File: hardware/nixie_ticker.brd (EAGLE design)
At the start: 124.1 x 49.5 mm, 12 parts

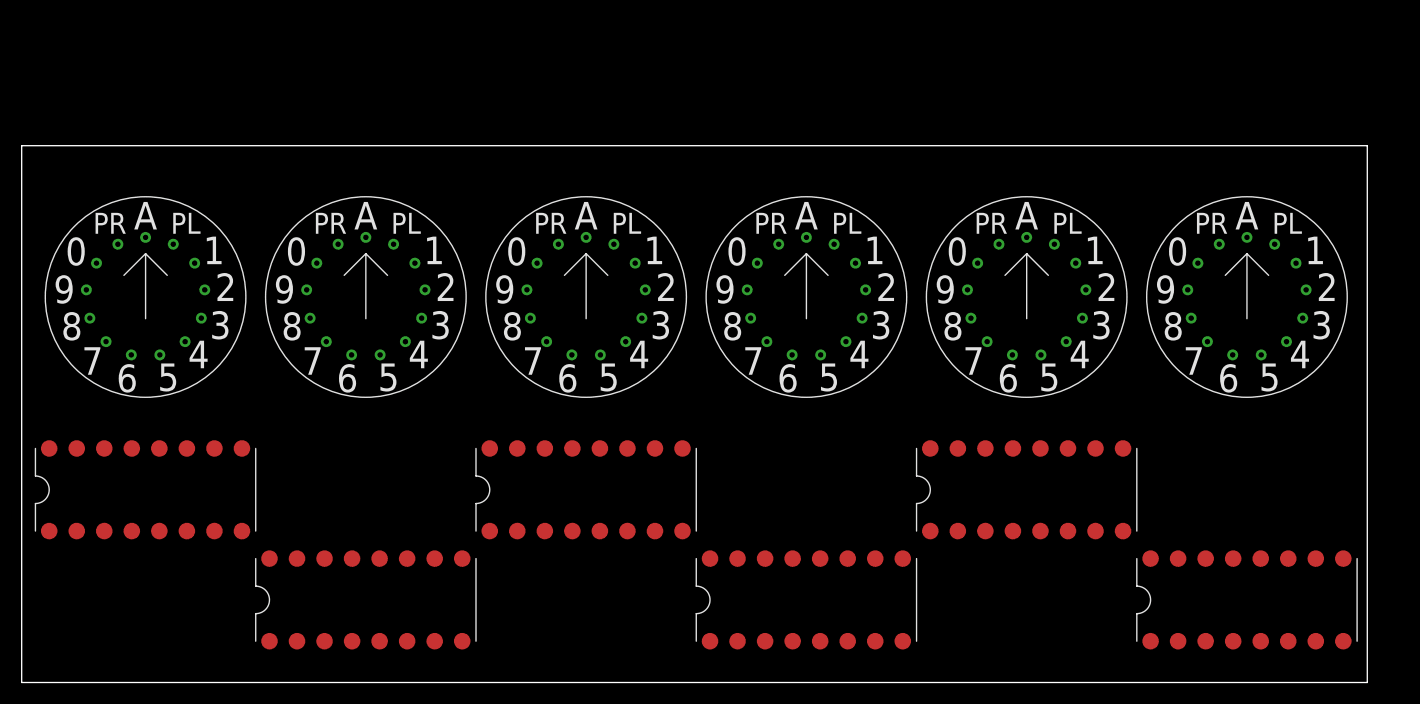
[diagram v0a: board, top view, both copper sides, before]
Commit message: Initial routing for first nixie
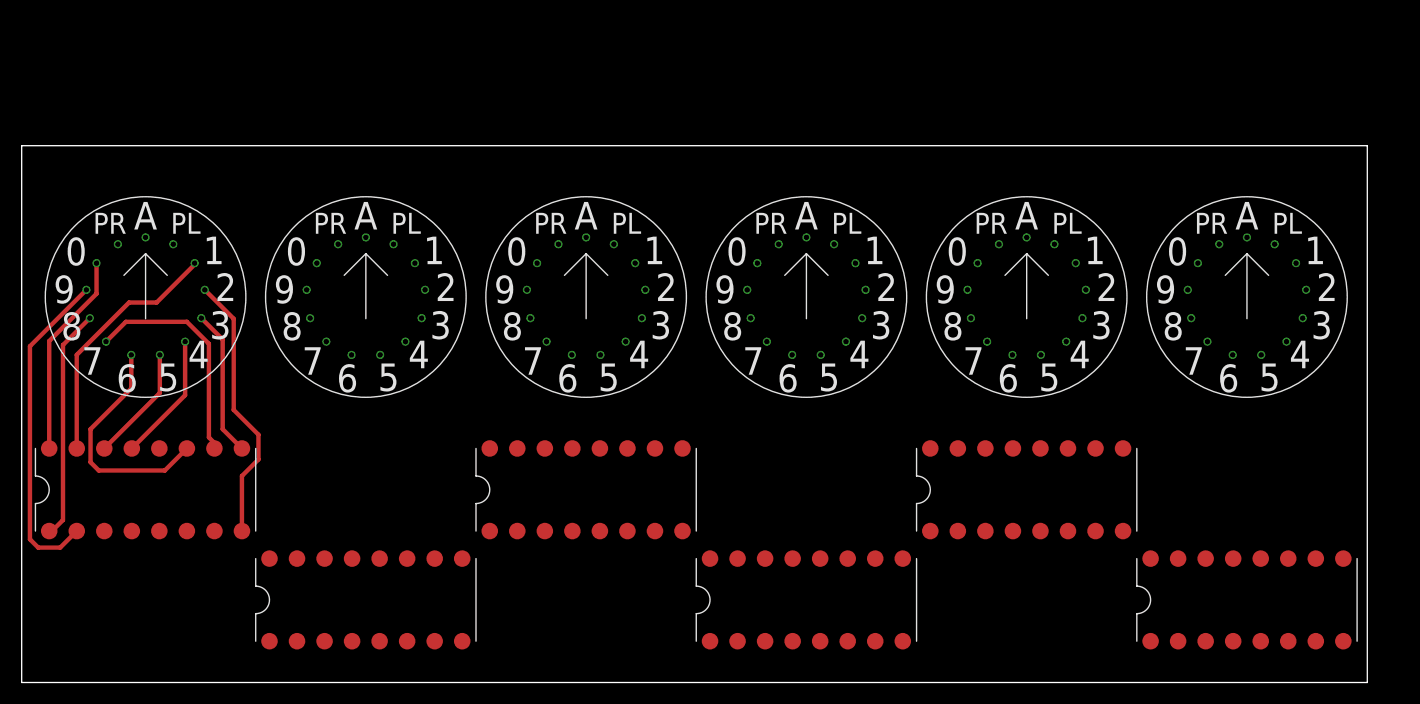
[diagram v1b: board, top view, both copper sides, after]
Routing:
- net N$10: track 0.00 -> 30.4 mm
- net N$3: track 0.00 -> 24.9 mm
- net N$2: track 0.00 -> 23.1 mm
- net N$7: track 0.00 -> 21.5 mm
- net N$9: track 0.00 -> 21.3 mm
- net N$8: track 0.00 -> 21.0 mm
- net N$1: track 0.00 -> 18.9 mm
- net N$4: track 0.00 -> 13.6 mm
- net N$5: track 0.00 -> 11.9 mm
- net N$6: track 0.00 -> 10.8 mm

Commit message: Wiring all nixie tubes using design blocks
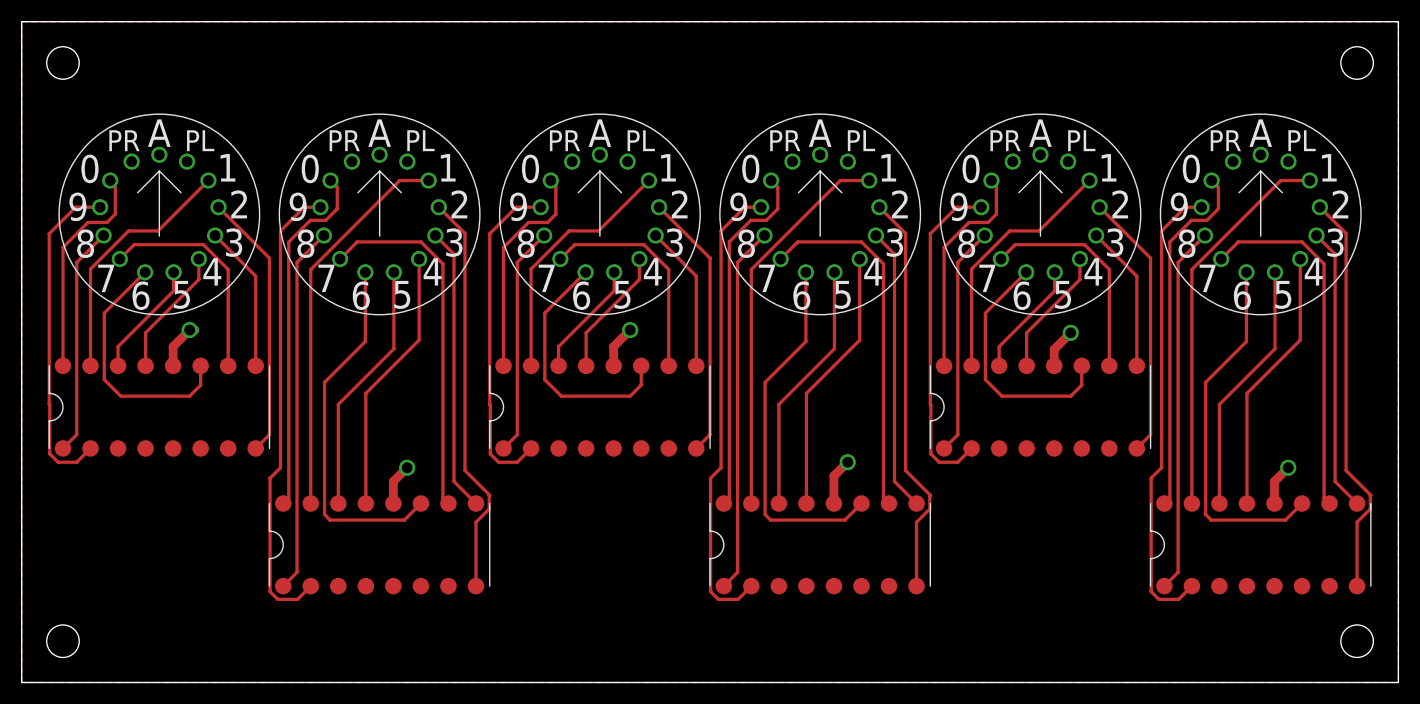
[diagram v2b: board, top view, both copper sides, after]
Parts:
- removed U$10, U$9: K155ID1, nixie_ticker:DIP-16_SMD
- removed U$3, U$4: IN14, nixie_ticker:IN14
- added U$15, U$19: IN14, nixie_ticker:IN14
- added U$16, U$20: K155ID1, nixie_ticker:DIP-16_SMD
- U$11: value K155ID1 -> IN14; device nixie_ticker:DIP-16_SMD -> nixie_ticker:IN14
- U$6: value IN14 -> K155ID1; device nixie_ticker:IN14 -> nixie_ticker:DIP-16_SMD
- moved U$6 60.5 mm to (53.3, 25.4), turned to 90 degrees
- moved U$5 40.1 mm to (53.3, 43.2)
- moved U$12 39.7 mm to (73.7, 12.7)
- moved U$11 31.8 mm to (73.7, 43.2), turned to 0 degrees
- moved U$2 7.73 mm to (33.0, 43.2)
- moved U$1 7.73 mm to (12.7, 43.2)
- moved U$7 7.73 mm to (12.7, 25.4)
- moved U$8 5.24 mm to (33.0, 12.7)
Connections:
- removed net N$21: U$3.P$12, U$9.P$16
- removed net N$22: U$3.P$3, U$9.P$15
- removed net N$23: U$3.P$4, U$9.P$8
- removed net N$24: U$3.P$5, U$9.P$9
- removed net N$25: U$3.P$6, U$9.P$13
- removed net N$26: U$3.P$7, U$9.P$14
- removed net N$27: U$3.P$8, U$9.P$11
- removed net N$28: U$3.P$9, U$9.P$10
- removed net N$29: U$3.P$10, U$9.P$1
- removed net N$30: U$3.P$11, U$9.P$2
- removed net N$41: U$11.P$16, U$5.P$12
- removed net N$42: U$11.P$15, U$5.P$3
- removed net N$43: U$11.P$8, U$5.P$4
- removed net N$44: U$11.P$9, U$5.P$5
- removed net N$45: U$11.P$13, U$5.P$6
- removed net N$46: U$11.P$14, U$5.P$7
- removed net N$47: U$11.P$11, U$5.P$8
- removed net N$48: U$11.P$10, U$5.P$9
- removed net N$49: U$11.P$1, U$5.P$10
- removed net N$50: U$11.P$2, U$5.P$11
- removed net N$51: U$12.P$16, U$6.P$12
- removed net N$52: U$12.P$15, U$6.P$3
- removed net N$53: U$12.P$8, U$6.P$4
- removed net N$54: U$12.P$9, U$6.P$5
- removed net N$55: U$12.P$13, U$6.P$6
- removed net N$56: U$12.P$14, U$6.P$7
- removed net N$57: U$12.P$11, U$6.P$8
- removed net N$58: U$12.P$10, U$6.P$9
- removed net N$59: U$12.P$1, U$6.P$10
- removed net N$60: U$12.P$2, U$6.P$11
- new net +5V: U$12.P$5, U$16.P$5, U$20.P$5, U$6.P$5, U$7.P$5, U$8.P$5
- new net GND: U$12.P$12, U$16.P$12, U$20.P$12, U$6.P$12, U$7.P$12, U$8.P$12
- new net N$100: U$15.P$11, U$16.P$2
- new net N$121: U$19.P$12, U$20.P$16
- new net N$122: U$19.P$3, U$20.P$15
- new net N$123: U$19.P$4, U$20.P$8
- new net N$124: U$19.P$5, U$20.P$9
- new net N$125: U$19.P$6, U$20.P$13
- new net N$126: U$19.P$7, U$20.P$14
- new net N$127: U$19.P$8, U$20.P$11
- new net N$128: U$19.P$9, U$20.P$10
- new net N$129: U$19.P$10, U$20.P$1
- new net N$130: U$19.P$11, U$20.P$2
- new net N$61: U$11.P$12, U$12.P$16
- new net N$62: U$11.P$3, U$12.P$15
- new net N$63: U$11.P$4, U$12.P$8
- new net N$64: U$11.P$5, U$12.P$9
- new net N$65: U$11.P$6, U$12.P$13
- new net N$66: U$11.P$7, U$12.P$14
- new net N$67: U$11.P$8, U$12.P$11
- new net N$68: U$11.P$9, U$12.P$10
- new net N$69: U$11.P$10, U$12.P$1
- new net N$70: U$11.P$11, U$12.P$2
- new net N$91: U$15.P$12, U$16.P$16
- new net N$92: U$15.P$3, U$16.P$15
- new net N$93: U$15.P$4, U$16.P$8
- new net N$94: U$15.P$5, U$16.P$9
- new net N$95: U$15.P$6, U$16.P$13
- new net N$96: U$15.P$7, U$16.P$14
- new net N$97: U$15.P$8, U$16.P$11
- new net N$98: U$15.P$9, U$16.P$10
- new net N$99: U$15.P$10, U$16.P$1
- net N$31: now also U$5.P$12, U$6.P$16; no longer U$10.P$16, U$4.P$12
- net N$32: now also U$5.P$3, U$6.P$15; no longer U$10.P$15, U$4.P$3
- net N$33: now also U$5.P$4, U$6.P$8; no longer U$10.P$8, U$4.P$4
- net N$34: now also U$5.P$5, U$6.P$9; no longer U$10.P$9, U$4.P$5
- net N$35: now also U$5.P$6, U$6.P$13; no longer U$10.P$13, U$4.P$6
- net N$36: now also U$5.P$7, U$6.P$14; no longer U$10.P$14, U$4.P$7
- net N$37: now also U$5.P$8, U$6.P$11; no longer U$10.P$11, U$4.P$8
- net N$38: now also U$5.P$9, U$6.P$10; no longer U$10.P$10, U$4.P$9
- net N$39: now also U$5.P$10, U$6.P$1; no longer U$10.P$1, U$4.P$10
- net N$40: now also U$5.P$11, U$6.P$2; no longer U$10.P$2, U$4.P$11
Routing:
- net N$130: track 0.00 -> 42.8 mm
- net N$70: track 0.00 -> 42.8 mm
- net N$20: track 0.00 -> 42.8 mm
- net N$13: track 0.00 -> 37.4 mm
- net N$63: track 0.00 -> 37.4 mm
- net N$123: track 0.00 -> 37.4 mm
- net N$62: track 0.00 -> 35.9 mm
- net N$122: track 0.00 -> 35.9 mm
- net N$12: track 0.00 -> 35.9 mm
- net N$69: track 0.00 -> 33.9 mm
- net N$19: track 0.00 -> 33.9 mm
- net N$129: track 0.00 -> 33.9 mm
- net N$67: track 0.00 -> 33.6 mm
- net N$127: track 0.00 -> 33.6 mm
- net N$17: track 0.00 -> 33.6 mm
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- added copper zone on layer 1, net +5V
- added copper zone on layer 16, net GND
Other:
- board size 124.1 x 49.5 mm -> 127 x 61 mm
